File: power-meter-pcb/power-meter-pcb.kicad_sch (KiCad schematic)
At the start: 17 parts, among them J1 Crank interconnect, J2 Debug, SW1 EN, SW2 BOOT, U1 ESP32-S3-WROOM-1, U2 P3T1755

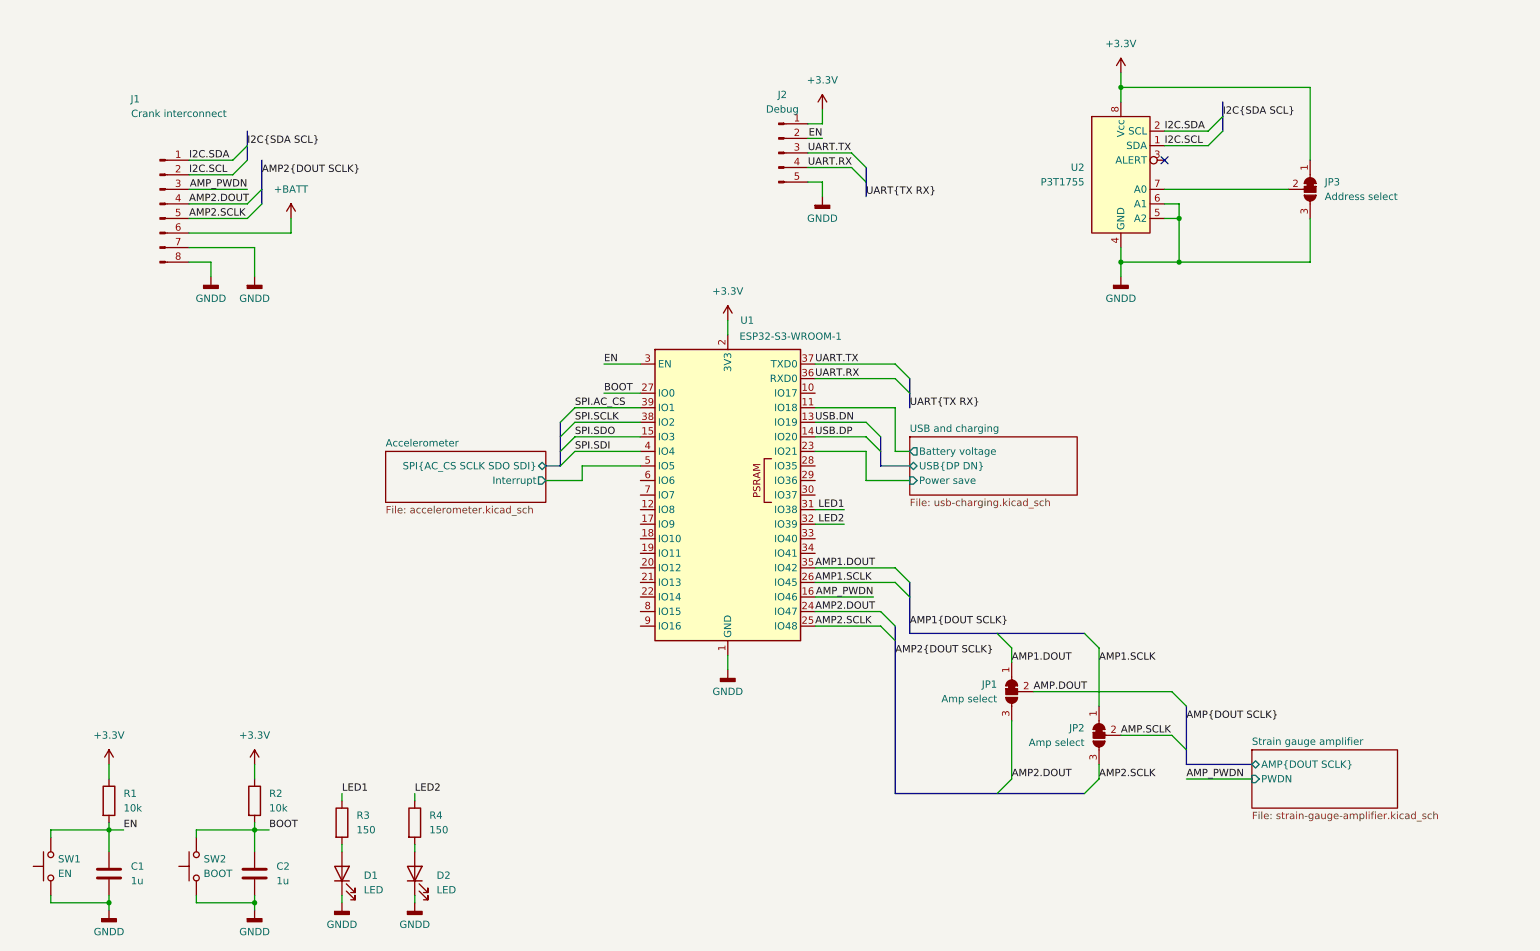
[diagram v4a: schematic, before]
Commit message: Adding filtering and pullup resistors, board layout
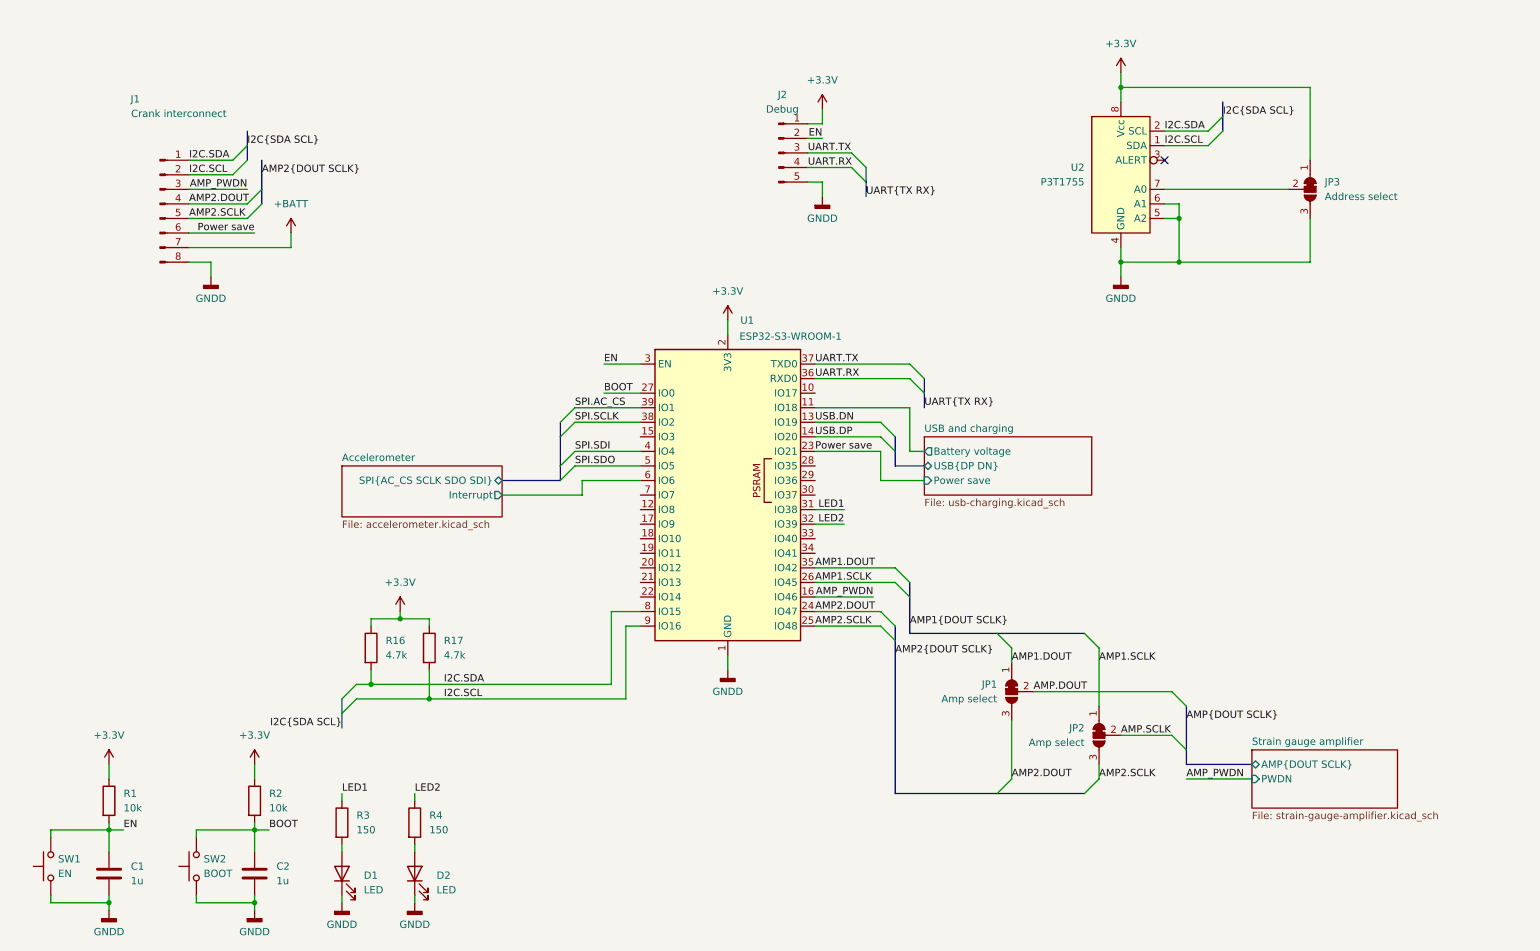
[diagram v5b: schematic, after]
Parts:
- added R16, R17: 4.7k, Resistor_SMD:R_0603_1608Metric_Pad0.98x0.95mm_HandSolder, symbol Device:R
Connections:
- net +3.3V: now also R16.1, R17.1
- net +BATT: now also J1.7 (Pin_7); no longer J1.6 (Pin_6)
- net Accelerometer/Interrupt: now also U1.6 (IO6); no longer U1.5 (IO5)
- net GNDD: no longer J1.7 (Pin_7)
- net I2C.SCL: now also U1.9 (IO16), R17.2
- net I2C.SDA: now also U1.8 (IO15), R16.2
- net SPI.SDO: now also U1.5 (IO5); no longer U1.15 (IO3)
- net USB and charging/Power save renamed Power save
- net Power save: now also J1.6 (Pin_6)

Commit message: Routing and component placement continues
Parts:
- J1: footprint Connector_PinHeader_2.54mm:PinHeader_1x08_P2.54mm_Vertical -> Connector_JST:JST_PH_B8B-PH-K_1x08_P2.00mm_Vertical
- renumbered R16 to R4, R4 to R5, R17 to R6
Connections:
- net AMP1.DOUT: now also U1.33 (IO40); no longer U1.35 (IO42)
- net AMP1.SCLK: now also U1.34 (IO41); no longer U1.26 (IO45)
- net AMP_PWDN: now also U1.35 (IO42); no longer U1.16 (IO46)
- net USB and charging/Charging: now reaches U1.10 (IO17)
- no-connect marks 1 -> 4
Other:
- sheet USB and charging ports: added Charging; removed none

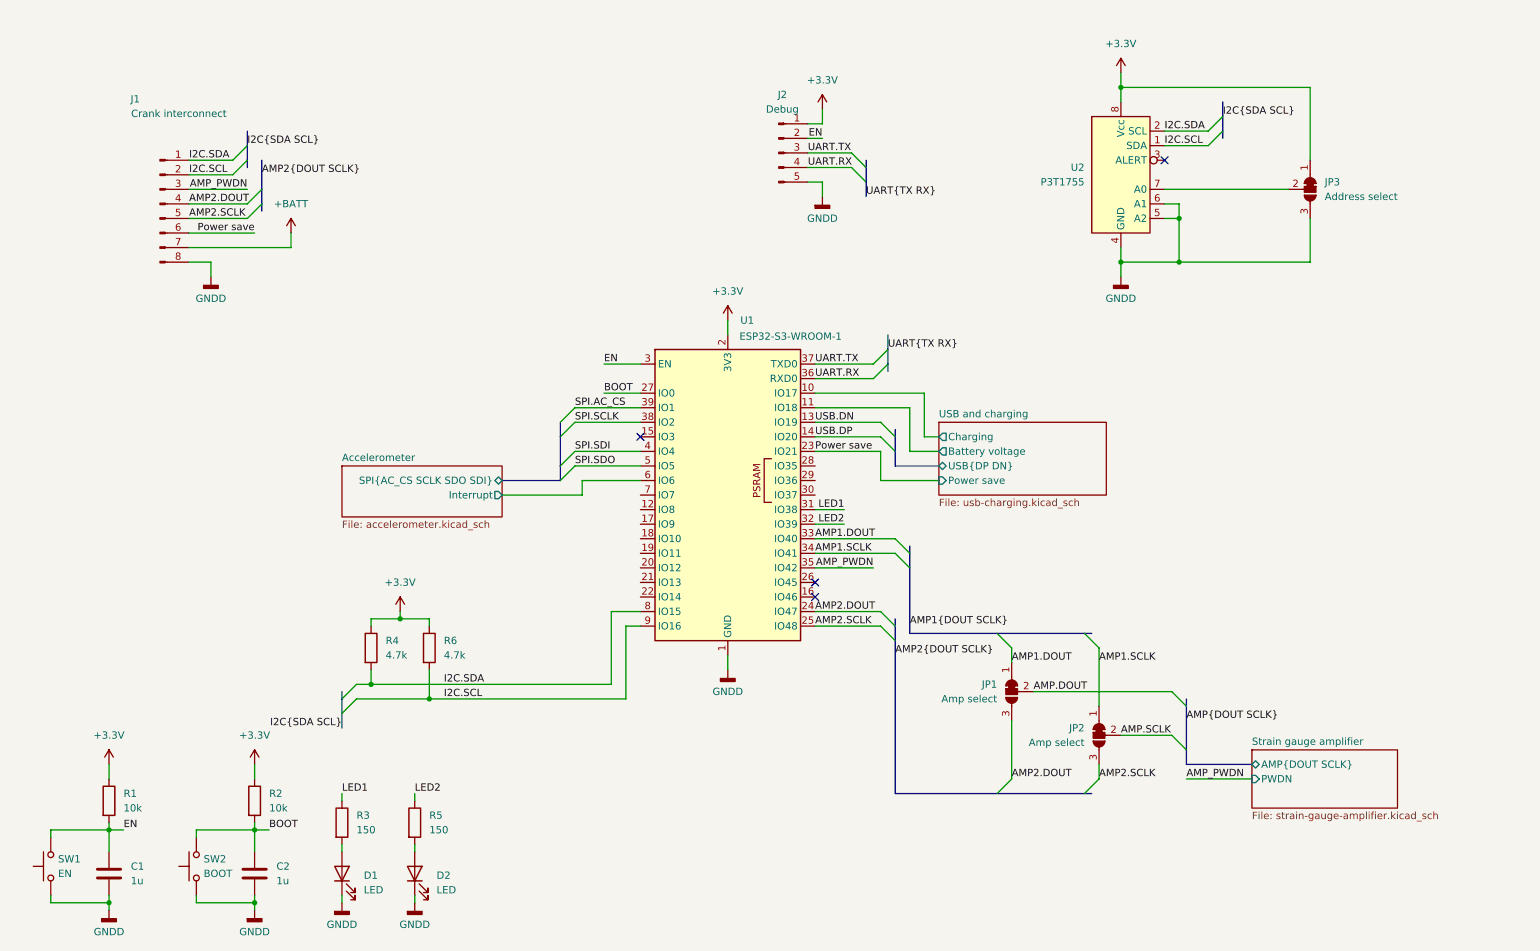
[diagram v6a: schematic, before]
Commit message: Tidying schematic
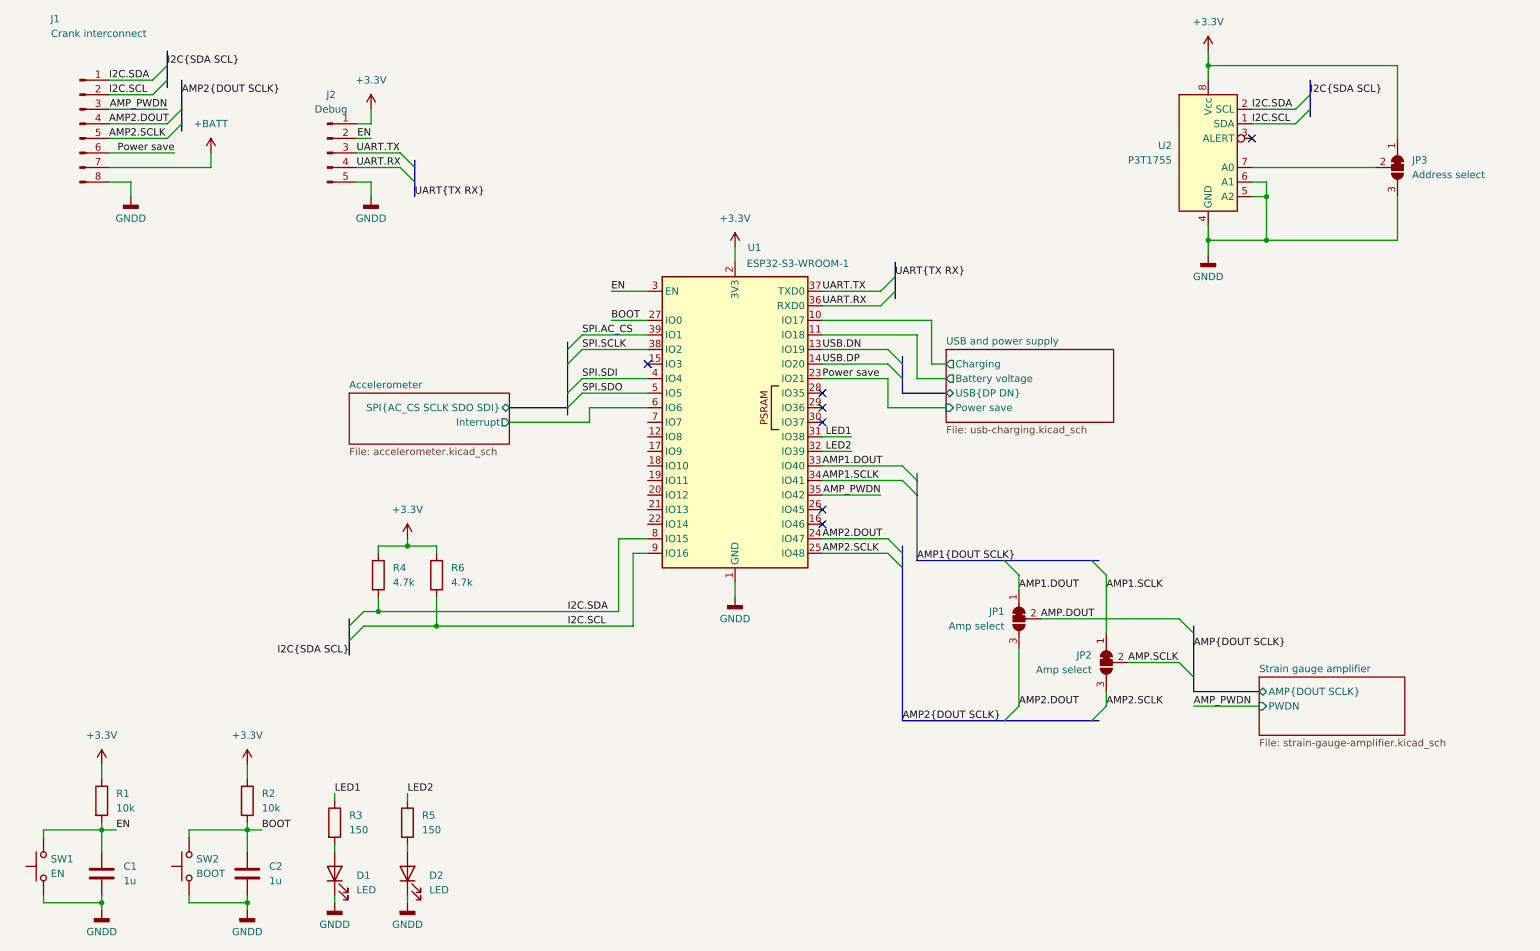
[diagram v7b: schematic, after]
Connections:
- no-connect marks 4 -> 7
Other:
- sheet USB and charging renamed USB and power supply
- moved on the sheet: C1, C2, D1, D2, J1, J2, JP1, JP2, JP3, R1, R2, R3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

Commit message: Improved board outline, in the middle of layout changes
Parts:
- added D3: LED, LED_SMD:LED_0603_1608Metric_Pad1.05x0.95mm_HandSolder, symbol Device:LED
- added H1, H2, H3, H4: MountingHole, MountingHole:MountingHole_2.2mm_M2, symbol Mechanical:MountingHole
- added R7: 150, Resistor_SMD:R_0603_1608Metric_Pad0.98x0.95mm_HandSolder, symbol Device:R
- J1: footprint Connector_JST:JST_PH_B8B-PH-K_1x08_P2.00mm_Vertical -> Connector_JST:JST_PH_S8B-PH-K_1x08_P2.00mm_Horizontal
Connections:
- net AMP1.DOUT: now also U1.31 (IO38); no longer U1.33 (IO40)
- net AMP1.SCLK: now also U1.32 (IO39); no longer U1.34 (IO41)
- net AMP_PWDN: now also U1.26 (IO45); no longer U1.35 (IO42)
- net GNDD: now also D3.1 (K)
- net LED1: now also U1.20 (IO12); no longer U1.31 (IO38)
- net LED2: now also U1.21 (IO13); no longer U1.32 (IO39)
- net LED3: now reaches U1.22 (IO14)
- net LED3: now also R7.1
- net USB.DN renamed USB.D_N
- net USB.DP renamed USB.D_P
- new net: D3.2 (A), R7.2
- no-connect marks 7 -> 14
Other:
- sheet USB and power supply ports: added USB{D_P D_N}; removed USB{DP DN}
- note added: "Mounting holes"
